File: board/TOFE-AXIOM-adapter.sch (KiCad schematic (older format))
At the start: 11 parts, among them CN1 C, U1 24AA01/24LC01B

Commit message: Converted to just the pins footprint.
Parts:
- TOFE1: footprint TOFE_8X_HalfHeight:TOFE_8X_HalfHeight -> TOFE_8X_Pins:TOFE_8X_Pins
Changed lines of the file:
@@
 F 0 "TOFE1" H 5200 2400 60  0000 C CNN
 F 1 "TOFE-8X" H 4550 2400 60  0000 C CNN
-F 2 "TOFE_8X_HalfHeight:TOFE_8X_HalfHeight" H 3900 4950 60  0001 C CNN
+F 2 "TOFE_8X_Pins:TOFE_8X_Pins" H 3900 4950 60  0001 C CNN
 F 3 "~" H 3900 4950 60  0000 C CNN
 	1    5200 5250

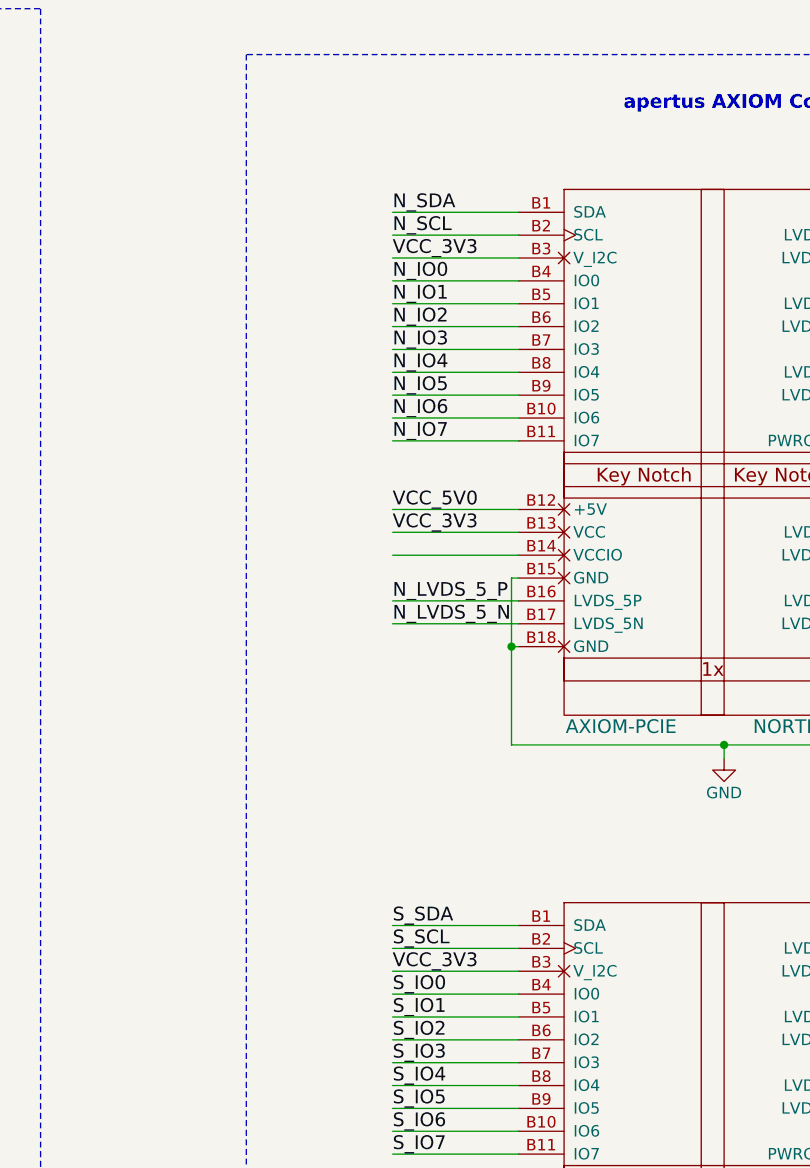
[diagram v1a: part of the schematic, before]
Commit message: Adding debug header for I2C lines.
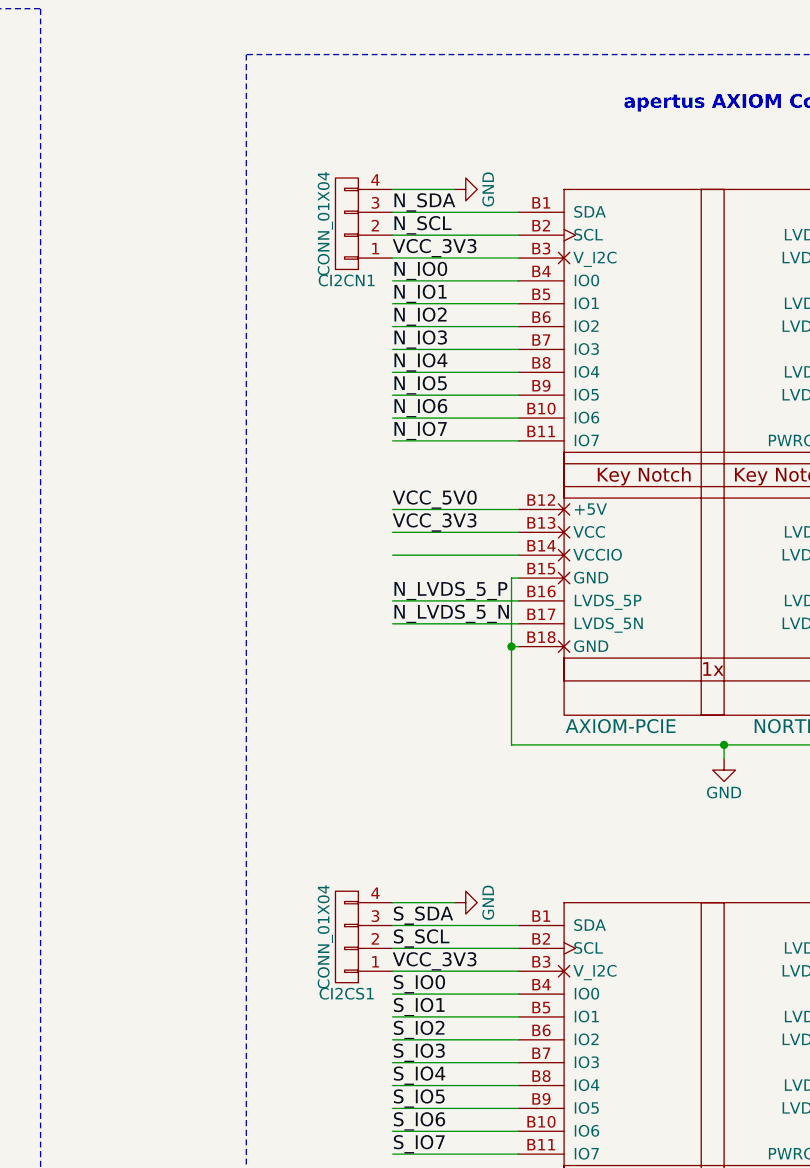
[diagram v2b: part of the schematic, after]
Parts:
- added CI2CN1, CI2CS1: CONN_01X04, symbol CONN_01X04
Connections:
- wire segments 213 -> 215
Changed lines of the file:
@@
 Text Label 8490 6910 0    60   ~ 0
 VCC_3V3
+$Comp
+L CONN_01X04 CI2CS1
+U 1 1 56EF47D9
+P 8290 5560
+F 0 "CI2CS1" H 8290 5810 50  0000 C CNN
+F 1 "CONN_01X04" V 8390 5560 50  0000 C CNN
+F 2 "" H 8290 5560 50  0000 C CNN
+F 3 "" H 8290 5560 50  0000 C CNN
+	1    8290 5560
+	-1   0    0    1
+$EndComp
+$Comp
+L CONN_01X04 CI2CN1
+U 1 1 56EF4942
+P 8290 2440
+F 0 "CI2CN1" H 8290 2690 50  0000 C CNN
+F 1 "CONN_01X04" V 8390 2440 50  0000 C CNN
+F 2 "" H 8290 2440 50  0000 C CNN
+F 3 "" H 8290 2440 50  0000 C CNN
+	1    8290 2440
+	-1   0    0    1
+$EndComp
+$Comp
+L GND #PWR?
+U 1 1 56EF4A15
+P 8760 2290
+F 0 "#PWR?" H 8760 2040 50  0001 C CNN
+F 1 "GND" H 8760 2140 50  0000 C CNN
+F 2 "" H 8760 2290 50  0000 C CNN
+F 3 "" H 8760 2290 50  0000 C CNN
+	1    8760 2290
+	0    -1   -1   0
+$EndComp
+Wire Wire Line
+	8760 2290 8490 2290
+$Comp
+L GND #PWR?
+U 1 1 56EF4B73
+P 8760 5410
+F 0 "#PWR?" H 8760 5160 50  0001 C CNN
+F 1 "GND" H 8760 5260 50  0000 C CNN
+F 2 "" H 8760 5410 50  0000 C CNN
+F 3 "" H 8760 5410 50  0000 C CNN
+	1    8760 5410
+	0    -1   -1   0
+$EndComp
+Wire Wire Line
+	8760 5410 8490 5410
 $EndSCHEMATC

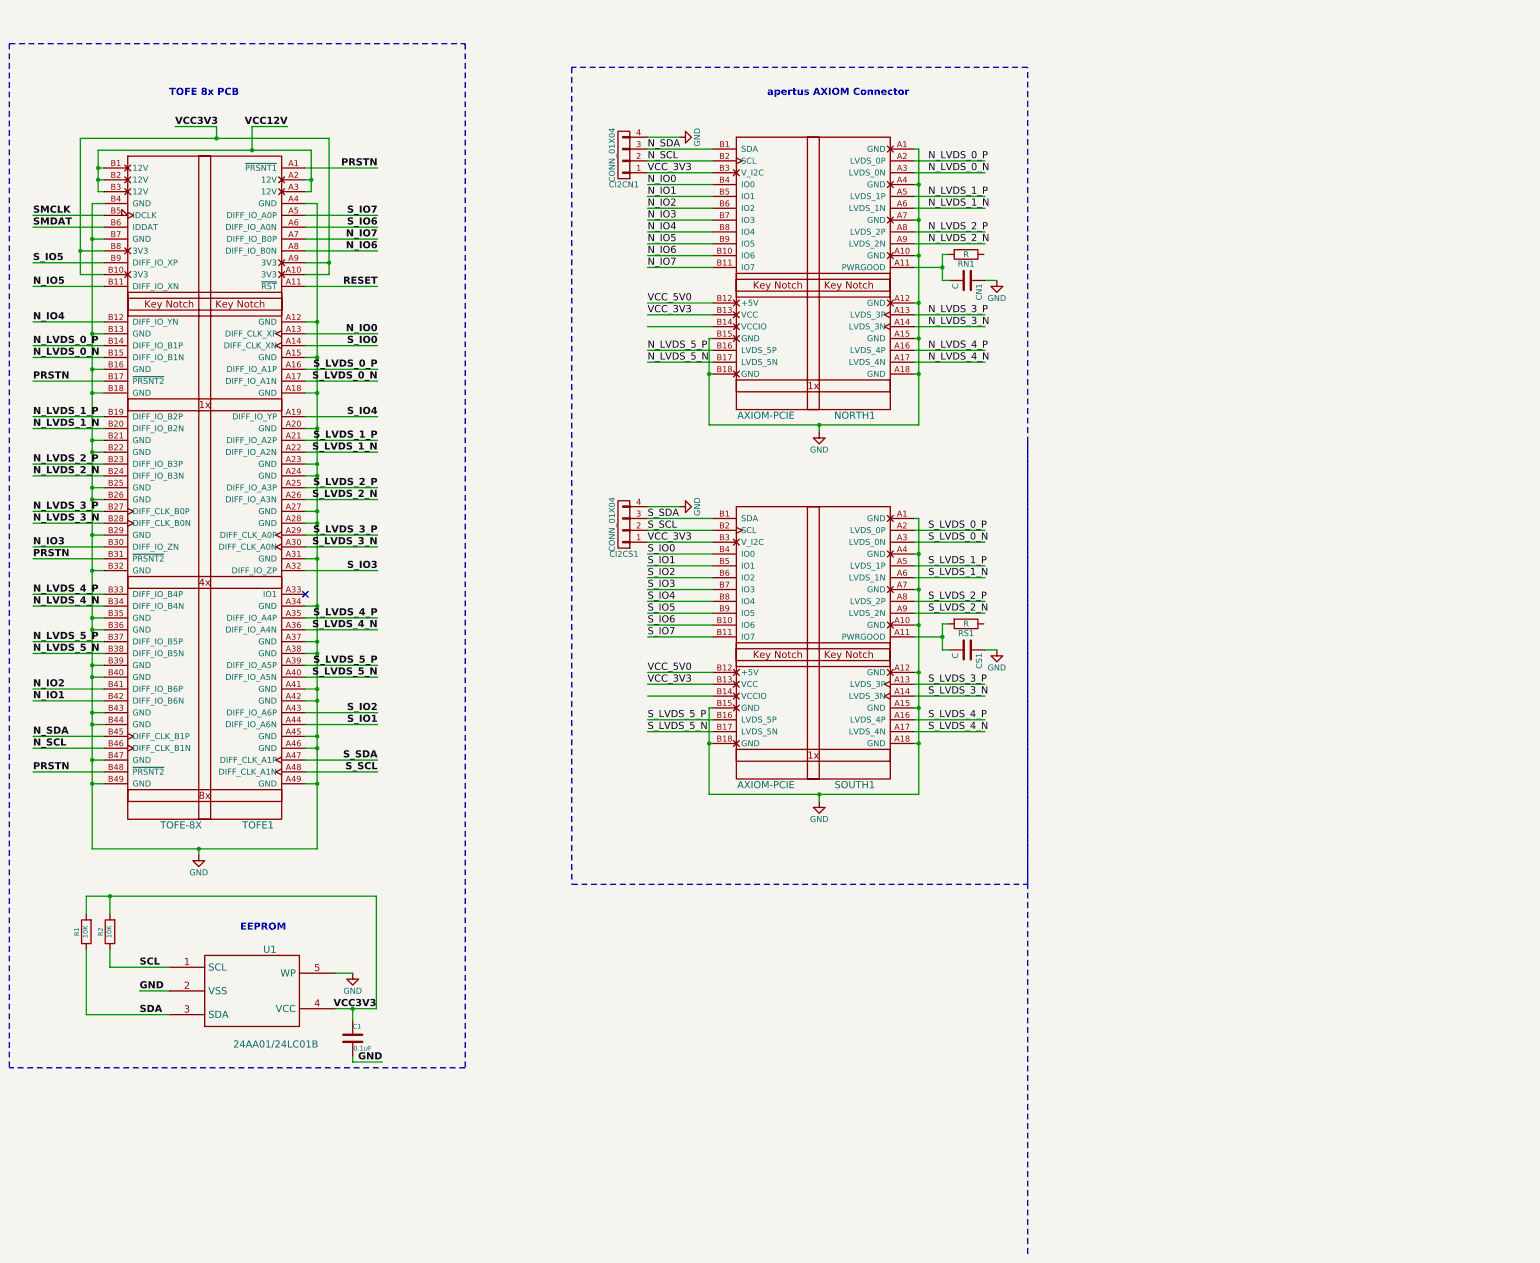
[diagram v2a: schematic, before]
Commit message: Adding 12V to 5V power supply.
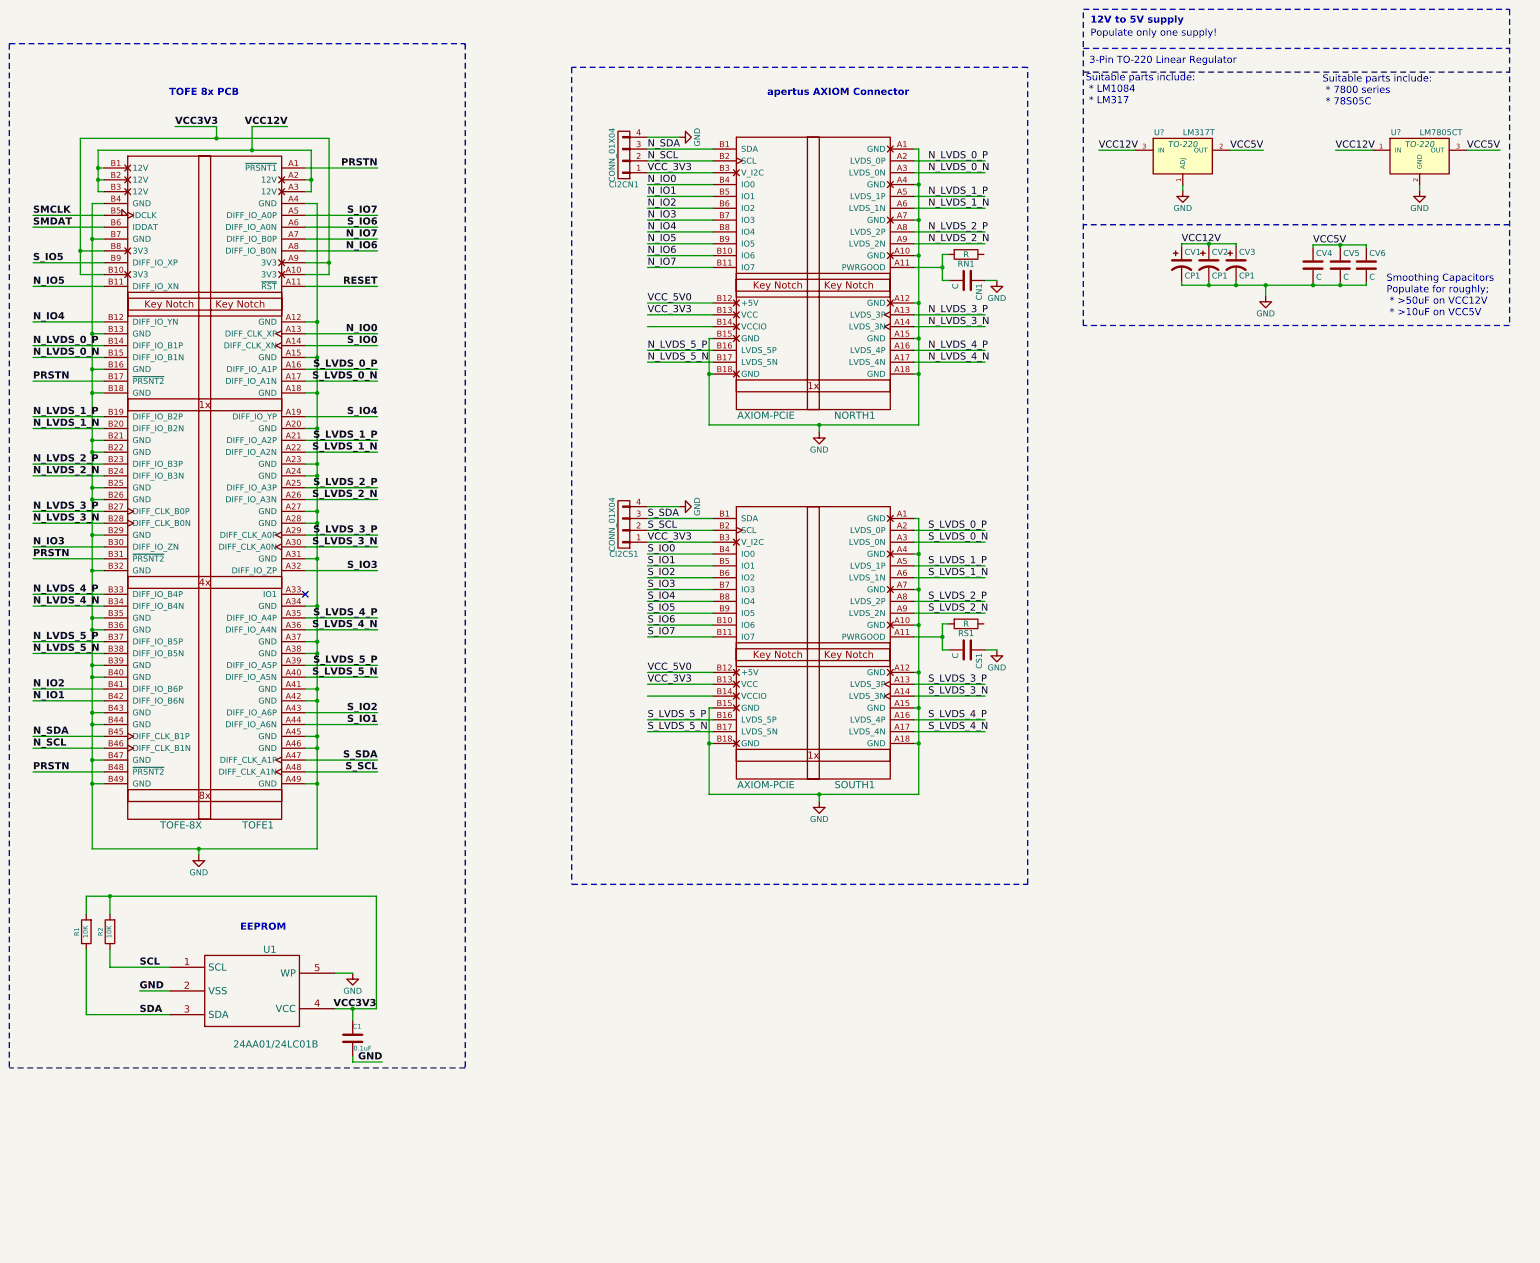
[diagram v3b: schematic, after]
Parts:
- added CV1, CV2, CV3: CP1, symbol CP1
- added CV4, CV5, CV6: C, symbol C
- added U?: LM317T, TO-220, symbol LM317T
- added U?: LM7805CT, TO-220, symbol LM7805CT
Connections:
- net labels added: VCC5V
- wire segments 215 -> 237
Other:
- note added: "12V to 5V supply"
- note added: "3-Pin TO-220 Linear Regulator"
- note added: "Populate only one supply!"
- note added: "Smoothing Capacitors\nPopulate for roughly;\n * >50uF on VCC12V\n * >10uF on VCC5V\n"
- note added: "Suitable parts include: \n * 7800 series\n * 78S05C"
- note added: "Suitable parts include: \n * LM1084\n * LM317"
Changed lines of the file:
@@
 	5600 2850 5700 2850
 Wire Wire Line
-	5700 2850 5700 8300
+	5700 8300 5700 2850
 Wire Wire Line
 	5700 4150 5600 4150
@@
 Connection ~ 5700 7450
 Wire Wire Line
-	5700 8300 3800 8300
+	3800 8300 5700 8300
 Connection ~ 3800 7750
 Connection ~ 5700 7750
@@
 	10740 2390 10780 2390
 Wire Wire Line
-	10780 2390 10780 4720
+	10780 4720 10780 2390
 Wire Wire Line
 	10740 2690 10780 2690
@@
 Connection ~ 10780 3690
 Wire Wire Line
-	10780 4720 9010 4720
+	9010 4720 10780 4720
 Connection ~ 10780 4290
 Wire Wire Line
 	9040 4290 9010 4290
 Wire Wire Line
-	9010 4720 9010 3990
+	9010 3990 9010 4720
 Wire Wire Line
 	9010 3990 9040 3990
@@
 	1    0    0    -1
 $EndComp
-Wire Notes Line
-	11700 11720 11700 4820
 Wire Wire Line
 	9040 5510 8490 5510
@@
 	10740 5510 10780 5510
 Wire Wire Line
-	10780 5510 10780 7840
+	10780 7840 10780 5510
 Wire Wire Line
 	10740 5810 10780 5810
@@
 Connection ~ 10780 6810
 Wire Wire Line
-	10780 7840 9010 7840
+	9010 7840 10780 7840
 Connection ~ 10780 7410
 Wire Wire Line
 	9040 7410 9010 7410
 Wire Wire Line
-	9010 7840 9010 7110
+	9010 7110 9010 7840
 Wire Wire Line
 	9010 7110 9040 7110
@@
 Wire Wire Line
 	8760 5410 8490 5410
+Wire Notes Line
+	12170 1210 15770 1210
+Wire Notes Line
+	15770 1210 15770 3880
+Wire Notes Line
+	15770 3880 12170 3880
+Wire Notes Line
+	12170 3880 12170 1210
+Text Notes 12230 1340 0    60   ~ 12
+12V to 5V supply
+Text Notes 12230 1450 0    60   ~ 0
+Populate only one supply!
+Text Notes 12220 1680 0    60   ~ 0
+3-Pin TO-220 Linear Regulator
+Wire Notes Line
+	12170 1540 15770 1540
+$Comp
+L LM317T U?
+U 1 1 56F236A7
+P 13010 2450
+F 0 "U?" H 12810 2650 50  0000 C CNN
+F 1 "LM317T" H 13010 2650 50  0000 L CNN
+F 2 "TO-220" H 13010 2550 50  0000 C CIN
+F 3 "" H 13010 2450 50  0000 C CNN
+	1    13010 2450
+	1    0    0    -1
+$EndComp
+$Comp
+L LM7805CT U?
+U 1 1 56F237BB
+P 15010 2450
+F 0 "U?" H 14810 2650 50  0000 C CNN
+F 1 "LM7805CT" H 15010 2650 50  0000 L CNN
+F 2 "TO-220" H 15010 2550 50  0000 C CIN
+F 3 "" H 15010 2450 50  0000 C CNN
+	1    15010 2450
+	1    0    0    -1
+$EndComp
+Text Notes 12190 2020 0    60   ~ 0
+Suitable parts include: \n * LM1084\n * LM317
+Text Notes 14190 2030 0    60   ~ 0
+Suitable parts include: \n * 7800 series\n * 78S05C
+Wire Notes Line
+	12170 1740 15770 1740
+$Comp
+L GND #PWR?
+U 1 1 56F23FEE
+P 15010 2740
+F 0 "#PWR?" H 15010 2490 50  0001 C CNN
+F 1 "GND" H 15010 2590 50  0000 C CNN
+F 2 "" H 15010 2740 50  0000 C CNN
+F 3 "" H 15010 2740 50  0000 C CNN
+	1    15010 2740
+	1    0    0    -1
+$EndComp
+$Comp
+L GND #PWR?
+U 1 1 56F2402D
+P 13010 2740
+F 0 "#PWR?" H 13010 2490 50  0001 C CNN
+F 1 "GND" H 13010 2590 50  0000 C CNN
+F 2 "" H 13010 2740 50  0000 C CNN
+F 3 "" H 13010 2740 50  0000 C CNN
+	1    13010 2740
+	1    0    0    -1
+$EndComp
+Wire Wire Line
+	13010 2740 13010 2700
+Wire Wire Line
+	15010 2740 15010 2700
+Wire Wire Line
+	14610 2400 14300 2400
+Text Label 14300 2400 0    60   ~ 0
+VCC12V
+Text Label 12300 2400 0    60   ~ 0
+VCC12V
+Wire Wire Line
+	12610 2400 12300 2400
+Text Label 13410 2400 0    60   ~ 0
+VCC5V
+Wire Wire Line
+	13410 2400 13690 2400
+Text Label 15410 2400 0    60   ~ 0
+VCC5V
+Wire Wire Line
+	15410 2400 15690 2400
+Text Label 13000 3190 0    60   ~ 0
+VCC12V
+Text Label 14110 3200 0    60   ~ 0
+VCC5V
+Wire Wire Line
+	13000 3190 13460 3190
+Wire Wire Line
+	14110 3200 14560 3200
+$Comp
+L GND #PWR?
+U 1 1 56F25B7E
+P 13710 3630
+F 0 "#PWR?" H 13710 3380 50  0001 C CNN
+F 1 "GND" H 13710 3480 50  0000 C CNN
+F 2 "" H 13710 3630 50  0000 C CNN
+F 3 "" H 13710 3630 50  0000 C CNN
+	1    13710 3630
+	1    0    0    -1
+$EndComp
+Wire Wire Line
+	13710 3540 13710 3630
+Wire Wire Line
+	13000 3540 14560 3540
+Connection ~ 13710 3540
+$Comp
+L CP1 CV3
+U 1 1 56F25E29
+P 13460 3360
+F 0 "CV3" H 13485 3460 50  0000 L CNN
+F 1 "CP1" H 13485 3260 50  0000 L CNN
+F 2 "" H 13460 3360 50  0000 C CNN
+F 3 "" H 13460 3360 50  0000 C CNN
+	1    13460 3360
+	1    0    0    -1
+$EndComp
+$Comp
+L C CV4
+U 1 1 56F25EDA
+P 14110 3370
+F 0 "CV4" H 14135 3470 50  0000 L CNN
+F 1 "C" H 14135 3270 50  0000 L CNN
+F 2 "" H 14148 3220 50  0000 C CNN
+F 3 "" H 14110 3370 50  0000 C CNN
+	1    14110 3370
+	1    0    0    -1
+$EndComp
+Wire Wire Line
+	13460 3190 13460 3210
+Wire Wire Line
+	13460 3540 13460 3510
+Wire Wire Line
+	14110 3200 14110 3220
+Wire Wire Line
+	14110 3540 14110 3520
+$Comp
+L C CV5
+U 1 1 56F26946
+P 14340 3370
+F 0 "CV5" H 14365 3470 50  0000 L CNN
+F 1 "C" H 14365 3270 50  0000 L CNN
+F 2 "" H 14378 3220 50  0000 C CNN
+F 3 "" H 14340 3370 50  0000 C CNN
+	1    14340 3370
+	1    0    0    -1
+$EndComp
+$Comp
+L C CV6
+U 1 1 56F269CE
+P 14560 3370
+F 0 "CV6" H 14585 3470 50  0000 L CNN
+F 1 "C" H 14585 3270 50  0000 L CNN
+F 2 "" H 14598 3220 50  0000 C CNN
+F 3 "" H 14560 3370 50  0000 C CNN
+	1    14560 3370
+	1    0    0    -1
+$EndComp
+Wire Wire Line
+	14340 3540 14340 3520
+Connection ~ 14110 3540
+Wire Wire Line
+	14560 3540 14560 3520
+Connection ~ 14340 3540
+Wire Wire Line
+	14560 3200 14560 3220
+Wire Wire Line
+	14340 3220 14340 3200
+Connection ~ 14340 3200
+$Comp
+L CP1 CV2
+U 1 1 56F27108
+P 13230 3360
+F 0 "CV2" H 13255 3460 50  0000 L CNN
+F 1 "CP1" H 13255 3260 50  0000 L CNN
+F 2 "" H 13230 3360 50  0000 C CNN
+F 3 "" H 13230 3360 50  0000 C CNN
+	1    13230 3360
+	1    0    0    -1
+$EndComp
+$Comp
+L CP1 CV1
+U 1 1 56F27198
+P 13000 3360
+F 0 "CV1" H 13025 3460 50  0000 L CNN
+F 1 "CP1" H 13025 3260 50  0000 L CNN
+F 2 "" H 13000 3360 50  0000 C CNN
+F 3 "" H 13000 3360 50  0000 C CNN
+	1    13000 3360
+	1    0    0    -1
+$EndComp
+Wire Wire Line
+	13230 3210 13230 3190
+Connection ~ 13230 3190
+Wire Wire Line
+	13000 3210 13000 3190
+Wire Wire Line
+	13000 3510 13000 3540
+Connection ~ 13460 3540
+Wire Wire Line
+	13230 3510 13230 3540
+Connection ~ 13230 3540
+Wire Notes Line
+	15770 3030 12170 3030
+Text Notes 14730 3810 0    60   ~ 0
+Smoothing Capacitors\nPopulate for roughly;\n * >50uF on VCC12V\n * >10uF on VCC5V\n
 $EndSCHEMATC
